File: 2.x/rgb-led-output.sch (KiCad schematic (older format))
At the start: 9 parts, among them K1 CONN_3, Q32 BSS138, U10 5V_SWITCHER

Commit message: Started layout on 2.0
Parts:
- removed U10: 5V_SWITCHER, ~, symbol 7805
- added U8: LM7805CT, TO-220, symbol LM7805CT
- C21: renamed from C23; value CP -> 10u; footprint ~ -> Capacitors_SMD:C_0805
- C22: renamed from C24; value CP -> 10u; footprint ~ -> Capacitors_SMD:C_0805
- K1: footprint (none) -> Socket_Strips:Socket_Strip_Straight_1x03
- Q32: footprint SOT-23 -> Housings_SOT-23_SOT-143_TSOT-6:SOT-23
- R135: renamed from R137; footprint ~ -> Resistors_SMD:R_0603
- R136: renamed from R138; footprint ~ -> Resistors_SMD:R_0603
- R137: renamed from R135; footprint ~ -> Resistors_SMD:R_0603
- R138: renamed from R136; footprint ~ -> Resistors_SMD:R_0603
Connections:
- net GND: now also U8.2 (GND)
- net RGB_12V: now also U8.1 (IN)
- net at C22.1, K1.1 (P1), R135.1: now also U8.3 (OUT)
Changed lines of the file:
@@
 LIBS:dips-s
 LIBS:nxp_armmcu
+LIBS:arm-swd-header
 LIBS:base-module-hardware-v2-cache
 EELAYER 25 0
@@
 $Descr USLetter 11000 8500
 encoding utf-8
-Sheet 7 7
+Sheet 7 8
 Title "DIYPinball Base Board"
-Date "2 apr 2014"
+Date "Sunday, February 22, 2015"
 Rev "2.0"
 Comp "DIYPinball.ca"
@@
 F 0 "Q32" H 4200 3851 40  0000 R CNN
 F 1 "BSS138" H 4200 4150 40  0000 R CNN
-F 2 "SOT-23" H 4070 4102 29  0000 C CNN
+F 2 "Housings_SOT-23_SOT-143_TSOT-6:SOT-23" H 4070 4102 29  0000 C CNN
 F 3 "~" H 4200 4000 60  0000 C CNN
 	1    4200 4000
@@
 $EndComp
 $Comp
-L GND #PWR61
+L GND #PWR057
 U 1 1 53278081
 P 4300 4850
-F 0 "#PWR61" H 4300 4850 30  0001 C CNN
+F 0 "#PWR057" H 4300 4850 30  0001 C CNN
 F 1 "GND" H 4300 4780 30  0001 C CNN
 F 2 "" H 4300 4850 60  0000 C CNN
@@
 $EndComp
 $Comp
-L R R135
+L R R137
 U 1 1 53278090
 P 3550 4050
-F 0 "R135" V 3630 4050 40  0000 C CNN
+F 0 "R137" V 3630 4050 40  0000 C CNN
 F 1 "22" V 3557 4051 40  0000 C CNN
-F 2 "~" V 3480 4050 30  0000 C CNN
+F 2 "Resistors_SMD:R_0603" V 3480 4050 30  0000 C CNN
 F 3 "~" H 3550 4050 30  0000 C CNN
 	1    3550 4050
@@
 $EndComp
 $Comp
-L R R136
+L R R138
 U 1 1 5327809F
 P 3900 4400
-F 0 "R136" V 3980 4400 40  0000 C CNN
+F 0 "R138" V 3980 4400 40  0000 C CNN
 F 1 "10K" V 3907 4401 40  0000 C CNN
-F 2 "~" V 3830 4400 30  0000 C CNN
+F 2 "Resistors_SMD:R_0603" V 3830 4400 30  0000 C CNN
 F 3 "~" H 3900 4400 30  0000 C CNN
 	1    3900 4400
@@
 	3900 4650 3900 4750
 Wire Wire Line
-	3900 4750 4300 4750
+	3900 4750 5100 4750
 Wire Wire Line
-	4300 4750 5100 4750
-Wire Wire Line
-	4300 4200 4300 4750
-Wire Wire Line
-	4300 4750 4300 4850
+	4300 4200 4300 4850
 Connection ~ 4300 4750
 Wire Wire Line
-	3800 4050 3900 4050
-Wire Wire Line
-	3900 4050 4000 4050
+	3800 4050 4000 4050
 Wire Wire Line
 	3900 4050 3900 4150
@@
 	3300 4050 2850 4050
 $Comp
-L R R138
+L R R136
 U 1 1 532780F3
 P 4650 3700
-F 0 "R138" V 4730 3700 40  0000 C CNN
+F 0 "R136" V 4730 3700 40  0000 C CNN
 F 1 "22" V 4657 3701 40  0000 C CNN
-F 2 "~" V 4580 3700 30  0000 C CNN
+F 2 "Resistors_SMD:R_0603" V 4580 3700 30  0000 C CNN
 F 3 "~" H 4650 3700 30  0000 C CNN
 	1    4650 3700
@@
 	4400 3700 4300 3700
 Wire Wire Line
-	4300 3600 4300 3700
-Wire Wire Line
-	4300 3700 4300 3800
+	4300 3600 4300 3800
 $Comp
-L R R137
+L R R135
 U 1 1 53278110
 P 4300 3350
-F 0 "R137" V 4380 3350 40  0000 C CNN
+F 0 "R135" V 4380 3350 40  0000 C CNN
 F 1 "1K" V 4307 3351 40  0000 C CNN
-F 2 "~" V 4230 3350 30  0000 C CNN
+F 2 "Resistors_SMD:R_0603" V 4230 3350 30  0000 C CNN
 F 3 "~" H 4300 3350 30  0000 C CNN
 	1    4300 3350
@@
 F 0 "K1" V 5550 3700 50  0000 C CNN
 F 1 "CONN_3" V 5650 3700 40  0000 C CNN
-F 2 "" H 5600 3700 60  0000 C CNN
+F 2 "Socket_Strips:Socket_Strip_Straight_1x03" H 5600 3700 60  0001 C BNN
 F 3 "" H 5600 3700 60  0000 C CNN
 	1    5600 3700
@@
 	4300 3000 4300 3100
 Wire Wire Line
-	3850 3000 3950 3000
-Wire Wire Line
-	3950 3000 4300 3000
-Wire Wire Line
-	4300 3000 5100 3000
+	3850 3000 5100 3000
 Wire Wire Line
 	5100 3000 5100 3600
@@
 	5100 3800 5100 4750
 $Comp
-L CP C24
+L CP C22
 U 1 1 5327816B
 P 3950 3300
-F 0 "C24" H 4000 3400 40  0000 L CNN
-F 1 "CP" H 4000 3200 40  0000 L CNN
-F 2 "~" H 4050 3150 30  0000 C CNN
+F 0 "C22" H 4000 3400 40  0000 L CNN
+F 1 "10u" H 4000 3200 40  0000 L CNN
+F 2 "Capacitors_SMD:C_0805" H 4050 3150 30  0001 C CNN
 F 3 "~" H 3950 3300 300 0000 C CNN
 	1    3950 3300
@@
 $EndComp
 $Comp
-L CP C23
+L CP C21
 U 1 1 5327817A
 P 2950 3300
-F 0 "C23" H 3000 3400 40  0000 L CNN
-F 1 "CP" H 3000 3200 40  0000 L CNN
-F 2 "~" H 3050 3150 30  0000 C CNN
+F 0 "C21" H 3000 3400 40  0000 L CNN
+F 1 "10u" H 3000 3200 40  0000 L CNN
+F 2 "Capacitors_SMD:C_0805" H 3050 3150 30  0001 C CNN
 F 3 "~" H 2950 3300 300 0000 C CNN
 	1    2950 3300
-	1    0    0    -1
-$EndComp
-$Comp
-L 7805 U10
-U 1 1 5327818B
-P 3450 3050
-F 0 "U10" H 3600 2854 60  0000 C CNN
-F 1 "5V_SWITCHER" H 3450 3250 60  0000 C CNN
-F 2 "~" H 3450 3050 60  0000 C CNN
-F 3 "~" H 3450 3050 60  0000 C CNN
-	1    3450 3050
 	1    0    0    -1
 $EndComp
@@
 Connection ~ 3950 3000
 Wire Wire Line
-	2850 3000 2950 3000
-Wire Wire Line
-	2950 3000 3050 3000
+	2850 3000 3050 3000
 Wire Wire Line
 	2950 3000 2950 3100
@@
 	2950 3500 2950 3600
 Wire Wire Line
-	2950 3600 3450 3600
-Wire Wire Line
-	3450 3600 3950 3600
+	2950 3600 3950 3600
 Wire Wire Line
 	3950 3600 3950 3500
 Wire Wire Line
-	3450 3300 3450 3600
-Wire Wire Line
-	3450 3600 3450 3700
+	3450 3300 3450 3700
 Connection ~ 3450 3600
 $Comp
-L GND #PWR60
+L GND #PWR058
 U 1 1 5327826E
 P 3450 3700
-F 0 "#PWR60" H 3450 3700 30  0001 C CNN
+F 0 "#PWR058" H 3450 3700 30  0001 C CNN
 F 1 "GND" H 3450 3630 30  0001 C CNN
 F 2 "" H 3450 3700 60  0000 C CNN
@@
 	1    0    0    -1
 $EndComp
+$Comp
+L LM7805CT U8
+U 1 1 556AB994
+P 3450 3050
+F 0 "U8" H 3250 3250 40  0000 C CNN
+F 1 "LM7805CT" H 3450 3250 40  0000 L CNN
+F 2 "TO-220" H 3450 3150 30  0000 C CIN
+F 3 "" H 3450 3050 60  0000 C CNN
+	1    3450 3050
+	1    0    0    -1
+$EndComp

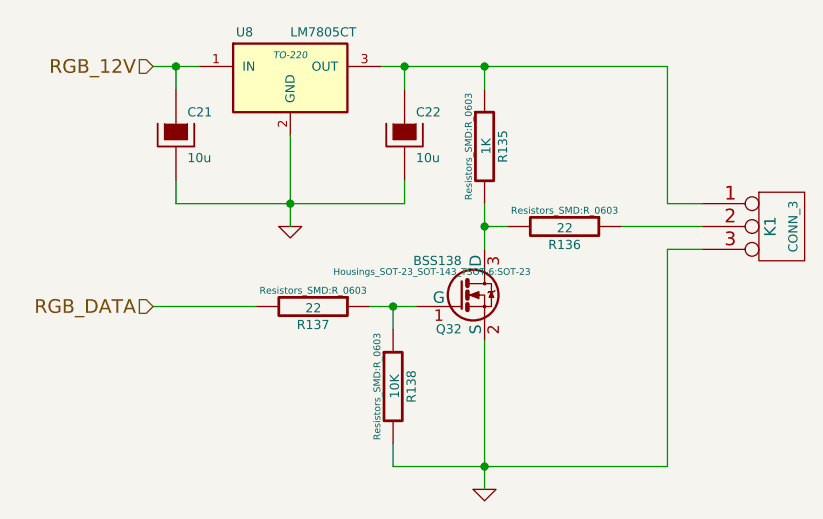
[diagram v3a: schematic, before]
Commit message: Fixing BAT54C pinout, and some feedback from layout review.
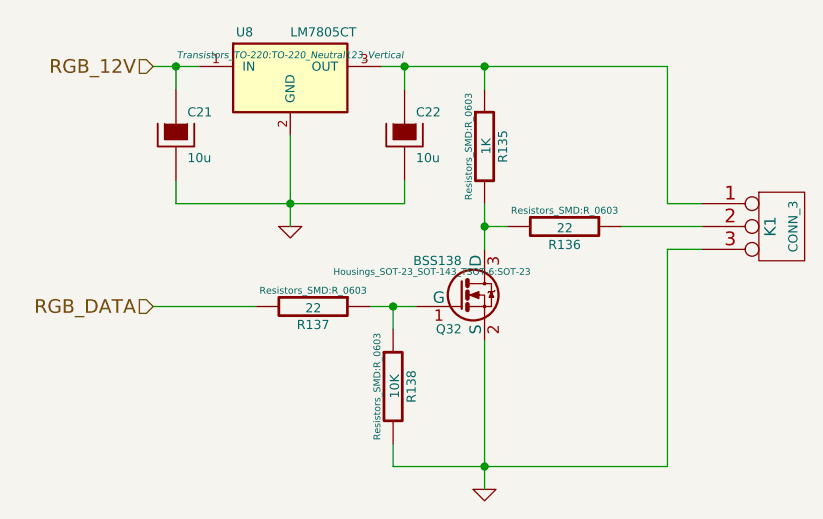
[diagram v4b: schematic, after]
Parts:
- U8: footprint TO-220 -> Transistors_TO-220:TO-220_Neutral123_Vertical
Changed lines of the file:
@@
 F 0 "U8" H 3250 3250 40  0000 C CNN
 F 1 "LM7805CT" H 3450 3250 40  0000 L CNN
-F 2 "TO-220" H 3450 3150 30  0000 C CIN
+F 2 "Transistors_TO-220:TO-220_Neutral123_Vertical" H 3450 3150 30  0000 C CIN
 F 3 "" H 3450 3050 60  0000 C CNN
 	1    3450 3050

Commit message: Committing latest files. This includes the KiCAD 4.0.0rc1 migration as well as the updates to Base Board 2.1.
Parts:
- C21, C22: symbol CP -> CP-RESCUE-base-module-hardware-v2
- R135, R136, R137, R138: symbol R -> R-RESCUE-base-module-hardware-v2
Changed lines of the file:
@@
 EESchema Schematic File Version 2
+LIBS:base-module-hardware-v2-rescue
 LIBS:power
 LIBS:device
@@
 LIBS:memory
 LIBS:xilinx
-LIBS:special
 LIBS:microcontrollers
 LIBS:dsp
@@
 $EndComp
 $Comp
-L GND #PWR057
+L GND-RESCUE-base-module-hardware-v2 #PWR059
 U 1 1 53278081
 P 4300 4850
-F 0 "#PWR057" H 4300 4850 30  0001 C CNN
+F 0 "#PWR059" H 4300 4850 30  0001 C CNN
 F 1 "GND" H 4300 4780 30  0001 C CNN
 F 2 "" H 4300 4850 60  0000 C CNN
@@
 $EndComp
 $Comp
-L R R137
+L R-RESCUE-base-module-hardware-v2 R137
 U 1 1 53278090
 P 3550 4050
@@
 $EndComp
 $Comp
-L R R138
+L R-RESCUE-base-module-hardware-v2 R138
 U 1 1 5327809F
 P 3900 4400
@@
 	3300 4050 2850 4050
 $Comp
-L R R136
+L R-RESCUE-base-module-hardware-v2 R136
 U 1 1 532780F3
 P 4650 3700
@@
 	4300 3600 4300 3800
 $Comp
-L R R135
+L R-RESCUE-base-module-hardware-v2 R135
 U 1 1 53278110
 P 4300 3350
@@
 	5100 3800 5100 4750
 $Comp
-L CP C22
+L CP-RESCUE-base-module-hardware-v2 C22
 U 1 1 5327816B
 P 3950 3300
@@
 $EndComp
 $Comp
-L CP C21
+L CP-RESCUE-base-module-hardware-v2 C21
 U 1 1 5327817A
 P 2950 3300
@@
 Connection ~ 3450 3600
 $Comp
-L GND #PWR058
+L GND-RESCUE-base-module-hardware-v2 #PWR060
 U 1 1 5327826E
 P 3450 3700
-F 0 "#PWR058" H 3450 3700 30  0001 C CNN
+F 0 "#PWR060" H 3450 3700 30  0001 C CNN
 F 1 "GND" H 3450 3630 30  0001 C CNN
 F 2 "" H 3450 3700 60  0000 C CNN
